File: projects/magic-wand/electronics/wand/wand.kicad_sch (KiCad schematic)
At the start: 44 parts, among them J1 USB-C-16P, J2 SM03B-SRSS-TB, J3 SM02B-SRSS-TB, SW1 PRESS_TO_ARM, U1 NINA-B302-00B-00, U2 LSM6DSV16XTR, U3 BQ25185DLHR, U4 TPS63900DSKR, U5 DRV2605LDGSR, U6 USBLC6-2SC6

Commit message: feat(magic-wand): freeze zero-error production routing
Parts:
- J1: BOM Comments Intentional 2.0 mm board-edge overhang; mechanical radial o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 -> Controlled board-edge overhang; mechanical radial opening d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
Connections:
- net HAPTIC_EN: now also U1.1 (P0.13); no longer U1.44 (P0.27)
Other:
- moved on the sheet: C_BAT, C_BUCK_IN, C_BUCK_OUT, C_CHG_IN, C_HAPTIC_REG, C_HAPTIC_VDD, C_IMU_IO, C_IMU_VDD, C_SYS, C_USB, F1, J1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

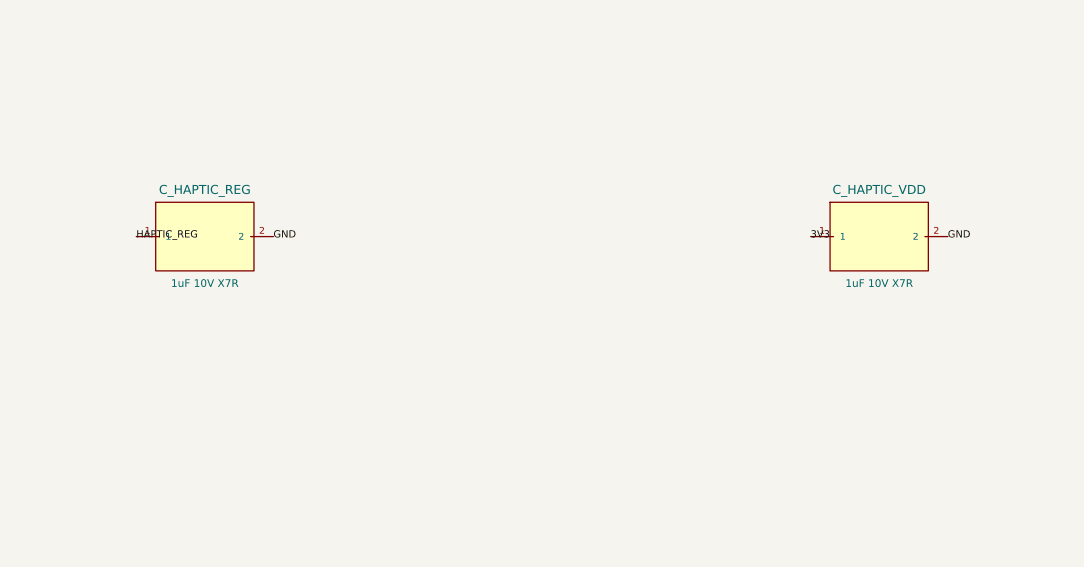
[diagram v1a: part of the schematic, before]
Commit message: feat(magic-wand): complete wand BOM LCSC 36/36 and rebuild JLC package
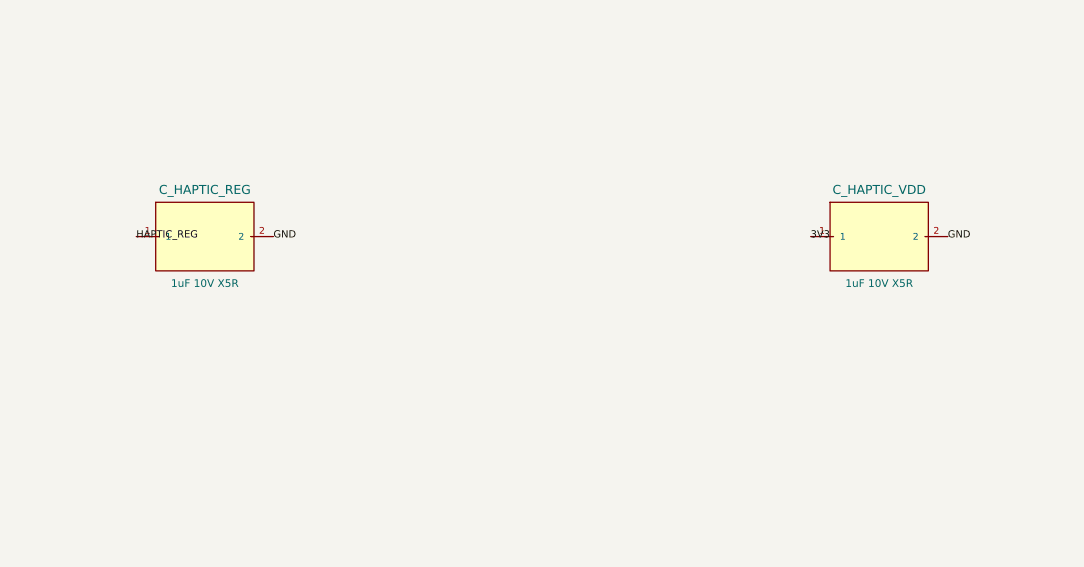
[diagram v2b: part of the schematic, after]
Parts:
- C_BAT, C_BUCK_IN, C_CHG_IN, C_SYS, C_USB: LCSC (none) -> C77073
- C_BUCK_OUT: LCSC (none) -> C77071
- C_HAPTIC_REG, C_HAPTIC_VDD: value 1uF 10V X7R -> 1uF 10V X5R; LCSC (none) -> C14445; MPN GRM155R71A105KE15D -> CL05A105KP5NNNC; Manufacturer Murata -> Samsung Electro-Mechanics
- C_IMU_IO, C_IMU_VDD: LCSC (none) -> C1525
- F1: LCSC (none) -> C210357
- J1: LCSC (none) -> C3197885
- J2: LCSC (none) -> C160403
- J3: LCSC (none) -> C160402
- L1: LCSC (none) -> C122469
- R_ARM, R_HAPTIC_EN: LCSC (none) -> C25741
- R_ARM_SER, R_ISET: LCSC (none) -> C106235
- R_CC1, R_CC2: LCSC (none) -> C25905
- R_CFG1: LCSC (none) -> C15011
- R_CFG2: LCSC (none) -> C17168
- R_CFG3: LCSC (none) -> C138050
- R_I2C_SCL, R_I2C_SDA: LCSC (none) -> C105871
- R_ILIM: LCSC (none) -> C138044
- R_STAT1, R_STAT2: LCSC (none) -> C25744
- SW1: LCSC (none) -> C202424
- U1: LCSC (none) -> C6335962
- U2: LCSC (none) -> C5267406
- U3: LCSC (none) -> C19725033
- U4: LCSC (none) -> C1518762
- U5: LCSC (none) -> C527464
- U6: LCSC (none) -> C7519
